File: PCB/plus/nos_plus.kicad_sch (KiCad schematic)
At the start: 159 parts, among them U1 PiPico_No_SWD, U2 ADG732BSUZ, U3 DC/DC

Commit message: Nos Pico+ PCB v1.0
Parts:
- removed U1: PiPico_No_SWD, nos_main:RPi_Pico_SMD_Pins_No_SWD, symbol nos_main:PiPico_No_SWD
- added D63: MBR120VLSF, Diode_SMD:D_SOD-123, symbol Device:D
- added SW1, SW2, SW3, SW4: SW_SPST, nos_plus:SW_Choc_V1V2_Cherry_MX_LED, symbol Switch:SW_SPST
- added U1: PiPico_No_SWD, nos_plus:RPi_Pico_SMD_Pins_No_SWD, symbol nos_plus:PiPico_No_SWD
- D1, D10, D11, D12, D13, D14, D15, D16, D17, D18, D19, D2, D20, D21, D22, D23, D24, D25, D26, D27, D28, D29, D3, D30, D31, D32, D33, D34, D35, D36, D37, D38, D39, D4, D40, D41, D42, D43, D44, D45, D46, D47, D48, D49, D5, D50, D51, D52, D53, D54, D55, D56, D57, D58, D59, D6, D60, D61, D62, D7, D8, D9: symbol nos_main:WS2812B_Unified -> nos_plus:WS2812B_Unified
- H1, H10, H11, H12, H13, H14, H15, H16, H17, H18, H19, H2, H20, H21, H22, H23, H24, H25, H26, H27, H28, H3, H4, H5, H6, H7, H8, H9: symbol nos_main:SS49E_SOT23 -> nos_plus:SS49E_SOT23
- U2: footprint nos_main:QFP50P900X900X120-49N -> nos_plus:QFP50P900X900X120-49N; symbol nos_main:ADG732BSUZ -> nos_plus:ADG732BSUZ
- U3: footprint nos_main:DCDC_3to5 -> nos_plus:DCDC_3to5
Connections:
- net +3V3: now also U1.36 (3V3)
- net +5V: now also D63.1 (K), U1.39 (VSYS)
- net A0: now also U1.29 (GPIO22)
- net A1: now also U1.27 (GPIO21)
- net A2: now also U1.26 (GPIO20)
- net A3: now also U1.25 (GPIO19)
- net A4: now also U1.24 (GPIO18)
- net CS: now also U1.22 (GPIO17)
- net GND: now also SW1.1 (A), SW2.1 (A), SW3.1 (A), SW4.1 (A), U1.13 (GND), U1.18 (GND), U1.23 (GND), U1.28 (GND), U1.3 (GND), U1.33 (AGND), U1.38 (GND), U1.8 (GND)
- net WR: now also U1.21 (GPIO16)
- net at USB1.5 (DN2), USB1.7 (DN1): now also U1.TP2 (USB1)
- net at USB1.6 (DP1), USB1.8 (DP2): now also U1.TP3 (USB2)
- net at D1.I (In): now also U1.4 (GPIO2)
- net at C30.1, R1.1, R2.2: now also U1.31 (GPIO26_ADC0), U1.32 (GPIO27_ADC1)
- net at D57.I (In): now also U1.1 (GPIO0)
- net VBUS: no longer names the net of USB1.11 (VBUS), USB1.2 (VBUS)
- net VBUS: now also D63.2 (A)
- new net: SW1.2 (B), U1.17 (GPIO13)
- new net: SW2.2 (B), U1.16 (GPIO12)
- new net: SW4.2 (B), U1.14 (GPIO10)
- new net: SW3.2 (B), U1.15 (GPIO11)
- no-connect marks 18 -> 19

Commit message: Nos Pico + PCB v1.01 (footprint finetune)
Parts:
- D63: footprint Diode_SMD:D_SOD-123 -> nos_plus:D_SOD-123_LONG
- H1, H10, H11, H12, H13, H14, H15, H16, H17, H18, H19, H2, H20, H21, H22, H23, H24, H25, H26, H27, H28, H3, H4, H5, H6, H7, H8, H9: footprint Package_TO_SOT_SMD:SOT-23-3 -> nos_plus:SOT-23-FAT
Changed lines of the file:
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@@
 			)
 		)
-		(property "Footprint" "Package_TO_SOT_SMD:SOT-23-3"
+		(property "Footprint" "nos_plus:SOT-23-FAT"
 			(at 383.54 187.325 0)
 			(effects
@@
 			)
 		)
-		(property "Footprint" "Package_TO_SOT_SMD:SOT-23-3"
+		(property "Footprint" "nos_plus:SOT-23-FAT"
 			(at 288.29 161.925 0)
 			(effects
@@
 			)
 		)
-		(property "Footprint" "Package_TO_SOT_SMD:SOT-23-3"
+		(property "Footprint" "nos_plus:SOT-23-FAT"
 			(at 307.34 161.925 0)
 			(effects
@@
 			)
 		)
-		(property "Footprint" "Package_TO_SOT_SMD:SOT-23-3"
+		(property "Footprint" "nos_plus:SOT-23-FAT"
 			(at 402.59 212.725 0)
 			(effects
@@
 			)
 		)
-		(property "Footprint" "Package_TO_SOT_SMD:SOT-23-3"
+		(property "Footprint" "nos_plus:SOT-23-FAT"
 			(at 364.49 238.125 0)
 			(effects
@@
 			)
 		)
-		(property "Footprint" "Package_TO_SOT_SMD:SOT-23-3"
+		(property "Footprint" "nos_plus:SOT-23-FAT"
 			(at 288.29 238.125 0)
 			(effects
@@
 			)
 		)
-		(property "Footprint" "Package_TO_SOT_SMD:SOT-23-3"
+		(property "Footprint" "nos_plus:SOT-23-FAT"
 			(at 307.34 187.325 0)
 			(effects
@@
 			)
 		)
-		(property "Footprint" "Package_TO_SOT_SMD:SOT-23-3"
+		(property "Footprint" "nos_plus:SOT-23-FAT"
 			(at 402.59 187.325 0)
 			(effects
@@
 			)
 		)
-		(property "Footprint" "Package_TO_SOT_SMD:SOT-23-3"
+		(property "Footprint" "nos_plus:SOT-23-FAT"
 			(at 288.29 212.725 0)
 			(effects
@@
 			)
 		)
-		(property "Footprint" "Package_TO_SOT_SMD:SOT-23-3"
+		(property "Footprint" "nos_plus:SOT-23-FAT"
 			(at 364.49 212.725 0)
 			(effects
@@
 			)
 		)
-		(property "Footprint" "Package_TO_SOT_SMD:SOT-23-3"
+		(property "Footprint" "nos_plus:SOT-23-FAT"
 			(at 345.44 212.725 0)
 			(effects
@@
 			)
 		)
-		(property "Description" ""
+		(property "Description" "Power symbol creates a global label with name \"GND\" , ground"
 			(at 325.755 55.88 0)
 			(effects
@@
 			)
 		)
-		(property "Footprint" "Package_TO_SOT_SMD:SOT-23-3"
+		(property "Footprint" "nos_plus:SOT-23-FAT"
 			(at 402.59 238.125 0)
 			(effects
@@
 			)
 		)
-		(property "Description" ""
+		(property "Description" "Resistor, small symbol"
 			(at 72.39 37.465 0)
 			(effects
@@
 			)
 		)
-		(property "Footprint" "Package_TO_SOT_SMD:SOT-23-3"
+		(property "Footprint" "nos_plus:SOT-23-FAT"
 			(at 307.34 238.125 0)
 			(effects
@@
 			)
 		)
-		(property "Footprint" "Package_TO_SOT_SMD:SOT-23-3"
+		(property "Footprint" "nos_plus:SOT-23-FAT"
 			(at 326.39 238.125 0)
 			(effects
@@
 			)
 		)
-		(property "Footprint" "Package_TO_SOT_SMD:SOT-23-3"
+		(property "Footprint" "nos_plus:SOT-23-FAT"
 			(at 345.44 161.925 0)
 			(effects
@@
 			)
 		)
-		(property "Footprint" "Package_TO_SOT_SMD:SOT-23-3"
+		(property "Footprint" "nos_plus:SOT-23-FAT"
 			(at 288.29 187.325 0)
 			(effects
@@
 			)
 		)
-		(property "Footprint" "Package_TO_SOT_SMD:SOT-23-3"
+		(property "Footprint" "nos_plus:SOT-23-FAT"
 			(at 383.54 161.925 0)
 			(effects
@@
 			)
 		)
-		(property "Footprint" "Package_TO_SOT_SMD:SOT-23-3"
+		(property "Footprint" "nos_plus:SOT-23-FAT"
 			(at 364.49 161.925 0)
 			(effects
@@
 			)
 		)
-		(property "Description" ""
+		(property "Description" "Power symbol creates a global label with name \"GND\" , ground"
 			(at 76.2 61.595 0)
 			(effects
@@
 			)
 		)
-		(property "Description" ""
+		(property "Description" "Resistor, small symbol"
 			(at 72.39 52.705 0)
 			(effects
@@
 			)
 		)
-		(property "Description" ""
+		(property "Description" "Generic connector, double row, 02x02, odd/even pin numbering scheme (row 1 odd numbers, row 2 even numbers), script generated (kicad-library-utils/schlib/autogen/connector/)"
 			(at 330.835 44.45 0)
 			(effects
@@
 			)
 		)
-		(property "Footprint" "Package_TO_SOT_SMD:SOT-23-3"
+		(property "Footprint" "nos_plus:SOT-23-FAT"
 			(at 326.39 161.925 0)
 			(effects
@@
 			)
 		)
-		(property "Footprint" "Package_TO_SOT_SMD:SOT-23-3"
+		(property "Footprint" "nos_plus:SOT-23-FAT"
 			(at 326.39 212.725 0)
 			(effects
@@
 			)
 		)
-		(property "Footprint" "Package_TO_SOT_SMD:SOT-23-3"
+		(property "Footprint" "nos_plus:SOT-23-FAT"
 			(at 326.39 187.325 0)
 			(effects
@@
 			)
 		)
-		(property "Footprint" "Package_TO_SOT_SMD:SOT-23-3"
+		(property "Footprint" "nos_plus:SOT-23-FAT"
 			(at 364.49 187.325 0)
 			(effects
@@
 			)
 		)
-		(property "Footprint" "Package_TO_SOT_SMD:SOT-23-3"
+		(property "Footprint" "nos_plus:SOT-23-FAT"
 			(at 345.44 238.125 0)
 			(effects
@@
 			)
 		)
-		(property "Footprint" "Diode_SMD:D_SOD-123"
+		(property "Footprint" "nos_plus:D_SOD-123_LONG"
 			(at 158.115 32.385 0)
 			(effects
@@
 			)
 		)
-		(property "Footprint" "Package_TO_SOT_SMD:SOT-23-3"
+		(property "Footprint" "nos_plus:SOT-23-FAT"
 			(at 402.59 161.925 0)
 			(effects
@@
 			)
 		)
-		(property "Footprint" "Package_TO_SOT_SMD:SOT-23-3"
+		(property "Footprint" "nos_plus:SOT-23-FAT"
 			(at 383.54 212.725 0)
 			(effects
@@
 			)
 		)
-		(property "Footprint" "Package_TO_SOT_SMD:SOT-23-3"
+		(property "Footprint" "nos_plus:SOT-23-FAT"
 			(at 383.54 238.125 0)
 			(effects
@@
 			)
 		)
-		(property "Footprint" "Package_TO_SOT_SMD:SOT-23-3"
+		(property "Footprint" "nos_plus:SOT-23-FAT"
 			(at 307.34 212.725 0)
 			(effects
@@
 			)
 		)
-		(property "Footprint" "Package_TO_SOT_SMD:SOT-23-3"
+		(property "Footprint" "nos_plus:SOT-23-FAT"
 			(at 345.44 187.325 0)
 			(effects
@@
 			)
 		)
-		(property "Description" ""
+		(property "Description" "Power symbol creates a global label with name \"+3V3\""
 			(at 323.215 36.195 0)
 			(effects

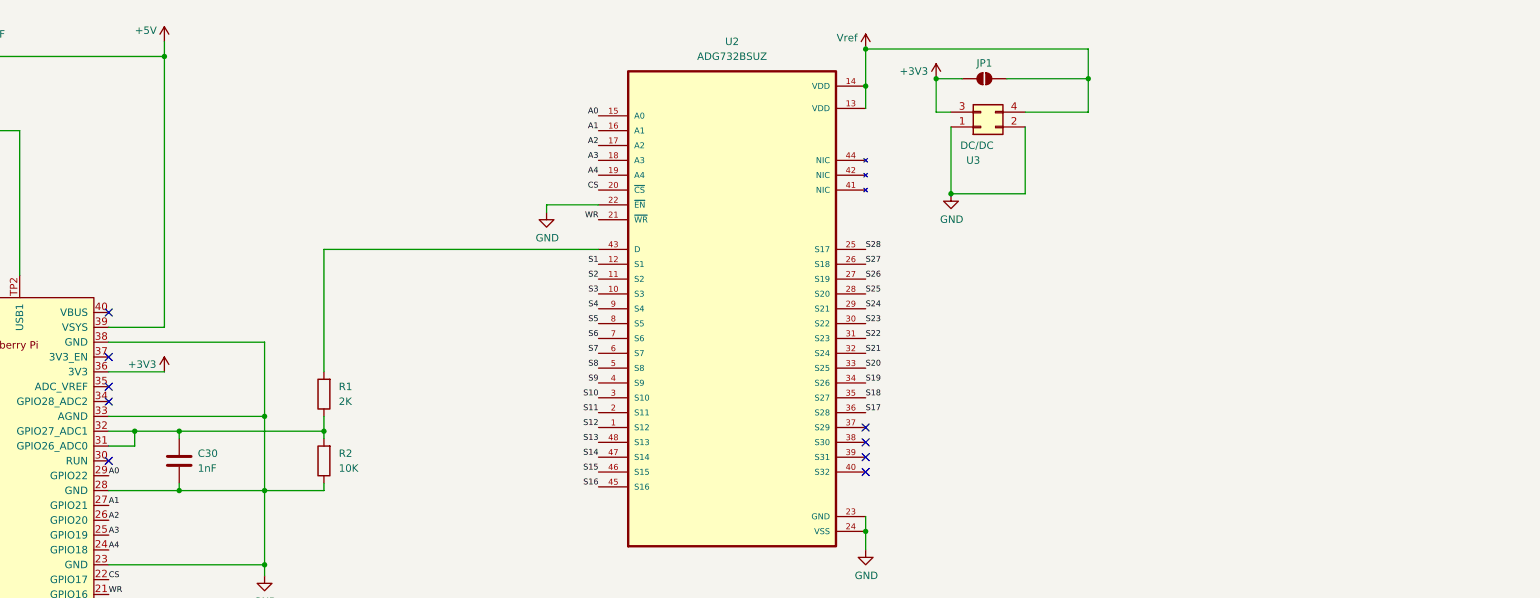
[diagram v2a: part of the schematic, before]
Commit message: PCB v1.2, remove unnecessary components
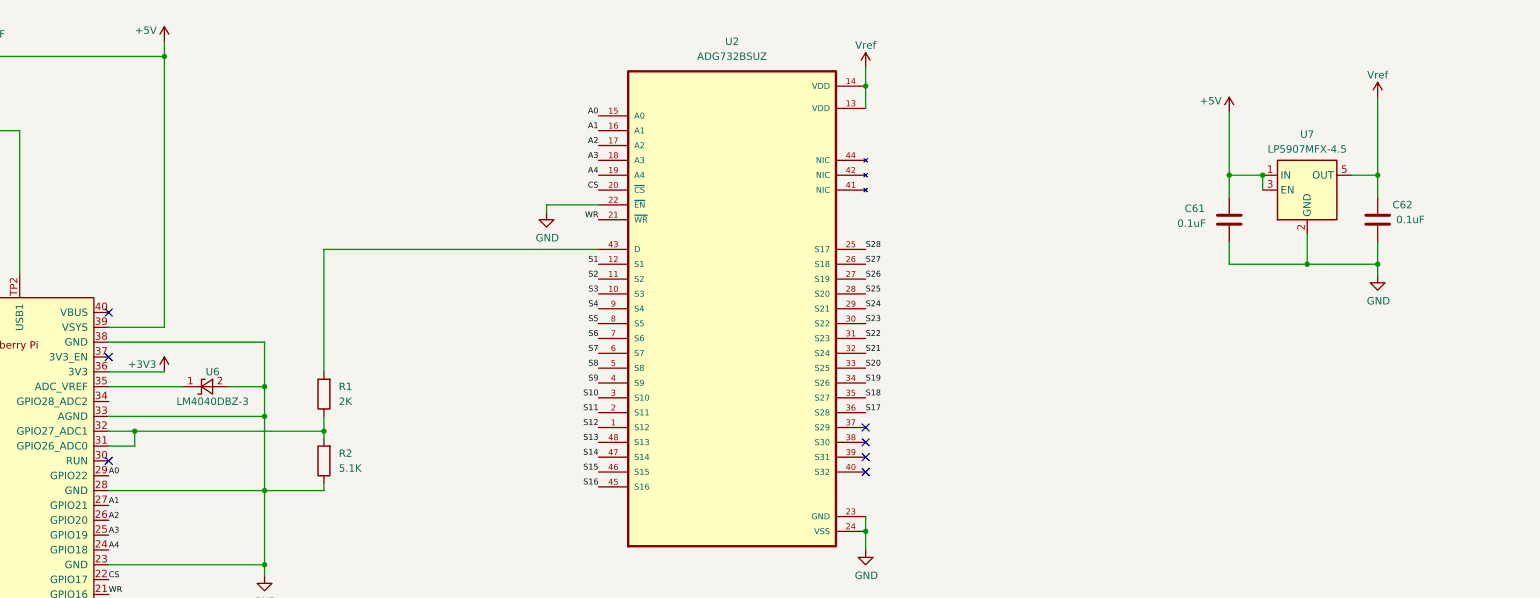
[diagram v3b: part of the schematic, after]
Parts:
- removed C30: 1nF, Capacitor_SMD:C_0603_1608Metric_Pad1.08x0.95mm_HandSolder, symbol Device:C
- removed JP1: SolderJumper_2_Open, Jumper:SolderJumper-2_P1.3mm_Open_RoundedPad1.0x1.5mm, symbol Jumper:SolderJumper_2_Open
- removed U3: DC/DC, nos_plus:DCDC_3to5, symbol Connector_Generic:Conn_02x02_Odd_Even
- added C61, C62: 0.1uF, Capacitor_SMD:C_0603_1608Metric_Pad1.08x0.95mm_HandSolder, symbol Device:C
- added U6: LM4040DBZ-3, nos_plus:SOT-23-FAT, symbol Reference_Voltage:LM4040DBZ-3
- added U7: LP5907MFX-4.5, Package_TO_SOT_SMD:SOT-23-5, symbol Regulator_Linear:LP5907MFX-4.5
- R2: value 10K -> 5.1K
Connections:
- net +5V: now also C61.1, U7.1 (IN), U7.3 (EN)
- net GND: now also C61.2, C62.2, U6.2 (A), U7.2 (GND)
- net Vref: now also C62.1, U7.5 (OUT)
- net at U1.35 (ADC_VREF): now also U6.1 (K)
- no-connect marks 19 -> 17
